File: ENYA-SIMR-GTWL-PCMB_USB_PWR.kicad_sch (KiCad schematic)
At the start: 47 parts, among them J1 USB_A_RA, J14 USB_WIRE_POINT, U1 USB2512B, U4 AP22653W6-7_ILIM_2.1A_SOT-23-6, U7 MCP1725_3.3V_500mA_DFN-8, U8 TPD2EUSB30_5.5V_8V_SOT-3, U9 TPD2EUSB30_5.5V_8V_SOT-3, Y1 ABM10_24MHz_10pF_SMD4_2.5x2.0

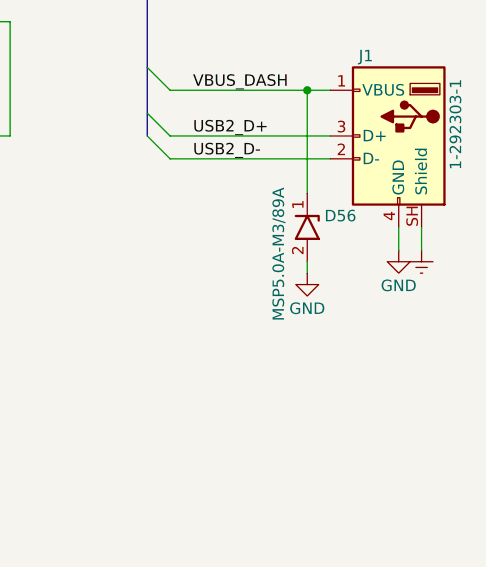
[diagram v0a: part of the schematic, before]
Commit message: rework for encoder instead of selector switch
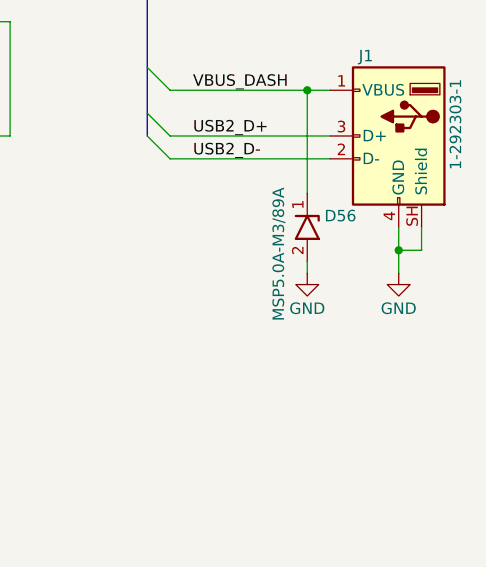
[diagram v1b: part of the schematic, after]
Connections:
- net Earth: no longer J1.SH (Shield)
- net GND: now also J1.SH (Shield)
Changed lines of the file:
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@@
     (comment 1 "ENYA-SIMR-GTWL-PCMB")
   )
+  (bus_alias "USB_DASH" (members "USB2_D+" "USB2_D-" "VBUS_DASH" "USB2_VBUS_EN" "nUSB2_VBUS_FAULT"))
   (bus_alias "USB_UP" (members "USB0_D+" "USB0_D-" "VBUS_DET"))
   (bus_alias "USB_WHEEL" (members "USB1_D+" "USB1_D-"))
-  (bus_alias "USB_DASH" (members "USB2_D+" "USB2_D-" "VBUS_DASH" "USB2_VBUS_EN" "nUSB2_VBUS_FAULT"))
   (junction (at 106.68 152.4) (diameter 0) (color 0 0 0 0)
   )
   (junction (at 93.98 175.26) (diameter 0) (color 0 0 0 0)
+  )
+  (junction (at 350.52 223.52) (diameter 0) (color 0 0 0 0)
   )
   (junction (at 73.66 157.48) (diameter 0) (color 0 0 0 0)
@@
     (stroke (width 0) (type default))
   )
+  (wire (pts (xy 350.52 223.52) (xy 350.52 226.06))
+    (stroke (width 0) (type default))
+  )
   (wire (pts (xy 259.08 96.52) (xy 261.62 96.52))
     (stroke (width 0) (type default))
@@
   )
   (wire (pts (xy 68.58 238.76) (xy 68.58 240.03))
+    (stroke (width 0) (type default))
+  )
+  (wire (pts (xy 350.52 223.52) (xy 353.06 223.52))
     (stroke (width 0) (type default))
   )
@@
     )
   )
-  (symbol (lib_id "power:GND") (at 350.52 223.52 0) (unit 1)
+  (symbol (lib_id "power:GND") (at 350.52 226.06 0) (unit 1)
     (in_bom yes) (on_board yes) (dnp no) (fields_autoplaced)
-    (property "Reference" "#PWR016" (at 350.52 229.87 0)
-      (effects (font (size 1.27 1.27)) hide)
-    )
-    (property "Value" "GND" (at 350.52 227.465 0)
-      (effects (font (size 1.27 1.27)))
-    )
-    (property "Footprint" "" (at 350.52 223.52 0)
-      (effects (font (size 1.27 1.27)) hide)
-    )
-    (property "Datasheet" "" (at 350.52 223.52 0)
+    (property "Reference" "#PWR016" (at 350.52 232.41 0)
+      (effects (font (size 1.27 1.27)) hide)
+    )
+    (property "Value" "GND" (at 350.52 230.005 0)
+      (effects (font (size 1.27 1.27)))
+    )
+    (property "Footprint" "" (at 350.52 226.06 0)
+      (effects (font (size 1.27 1.27)) hide)
+    )
+    (property "Datasheet" "" (at 350.52 226.06 0)
       (effects (font (size 1.27 1.27)) hide)
     )
@@
         )
       )
-    )
-  )
-  (symbol (lib_id "power:Earth") (at 353.06 223.52 0) (unit 1)
-    (in_bom yes) (on_board yes) (dnp no) (fields_autoplaced)
-    (property "Reference" "#PWR0103" (at 353.06 229.87 0)
-      (effects (font (size 1.27 1.27)) hide)
-    )
-    (property "Value" "Earth" (at 353.06 227.33 0)
-      (effects (font (size 1.27 1.27)) hide)
-    )
-    (property "Footprint" "" (at 353.06 223.52 0)
-      (effects (font (size 1.27 1.27)) hide)
-    )
-    (property "Datasheet" "~" (at 353.06 223.52 0)
-      (effects (font (size 1.27 1.27)) hide)
-    )
-    (pin "1")
-    (instances
-      (project "ENYA-SIMR-GTWL-PCMB"
-        (path "/6b1a3db9-0352-475b-af94-e6d69f246eea/cb59d8ca-9b58-4463-88f2-0a4f8455ba75"
-          (reference "#PWR0103") (unit 1)
-        )
-      )
